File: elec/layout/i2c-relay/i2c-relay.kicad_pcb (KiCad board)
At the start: 2 copper layers, 7 parts, among them U2 10kΩ ±1% 62.5mW, U3 1kΩ ±1% 62.5mW, U5 1kΩ ±1% 62.5mW

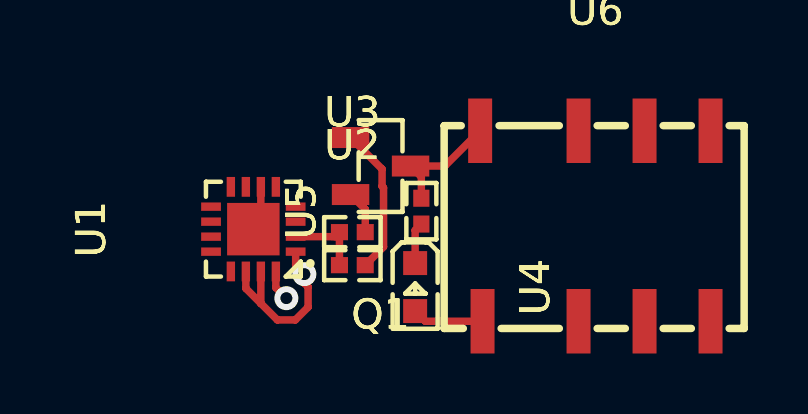
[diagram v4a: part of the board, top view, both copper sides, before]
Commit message: core layout, rebuild modules with compiler updates
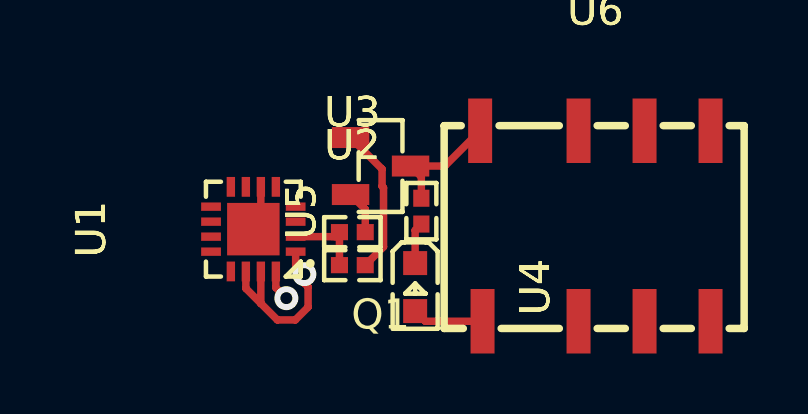
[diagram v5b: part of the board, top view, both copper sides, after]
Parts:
- Q1: footprint lib:SOT-23-3_L2.9-W1.3-P1.90-LS2.4-BR -> atopile:SOT-23-3_L2.9-W1.3-P1.90-LS2.4-BR-688f29
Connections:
- net gate renamed relay.fet.footprint.pins[0].net-net
- Q1 pad 2: gnd-1 -> gnd-3
- U1 pad 16: gnd-2 -> gnd-1
- U1 pad 17: gnd-2 -> gnd-1
- U1 pad 3: gpio_expander-net-3 -> gpio_expander-net-5
- U1 pad 4: gpio_expander-net-2 -> gpio_expander-net-6
- U1 pad 5: gpio_expander-net -> gpio_expander-net-3
- U1 pad 6: gnd-2 -> gnd-1
- U1 pad 7: gpio_expander-net-1 -> gpio_expander-net
- U1 pad 8: gpio_expander-net-6 -> gpio_expander-net-1
- U1 pad 9: gpio_expander-net-5 -> gpio_expander-net-2
- U3 pad 2: gnd-1 -> gnd-3
- U6 pad 4: gnd-3 -> gnd-2
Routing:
- net gnd-2: track 2.55 -> 0.00 mm, vias 1 -> 0
- net gnd-3: track 0.00 -> 1.46 mm
- net gnd-1: track 1.46 -> 2.55 mm, vias 0 -> 1
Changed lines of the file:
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@@
             (outputdirectory "")))
     (net 0 "")
-    (net 1 "gpio_expander-net-2")
+    (net 1 "gpio_expander-net-6")
     (net 2 "line-1")
     (net 3 "gpio_expander-net-4")
     (net 4 "hv")
-    (net 5 "gpio_expander-net-1")
-    (net 6 "gpio_expander-net-5")
+    (net 5 "gpio_expander-net")
+    (net 6 "gpio_expander-net-2")
     (net 7 "anode")
     (net 8 "input")
     (net 9 "gnd")
     (net 10 "INT")
-    (net 11 "gpio_expander-net-6")
+    (net 11 "gpio_expander-net-1")
     (net 12 "VCCI")
     (net 13 "hv-1")
     (net 14 "line")
-    (net 15 "gpio_expander-net")
-    (net 16 "gnd-3")
-    (net 17 "gnd-1")
+    (net 15 "gpio_expander-net-3")
+    (net 16 "gnd-2")
+    (net 17 "gnd-3")
     (net 18 "cathode")
     (net 19 "relay-gnd")
-    (net 20 "gate")
-    (net 21 "gpio_expander-net-3")
-    (net 22 "gnd-2")
+    (net 20 "relay.fet.footprint.pins[0].net-net")
+    (net 21 "gpio_expander-net-5")
+    (net 22 "gnd-1")
     (footprint "atopile:R0402-56259e"
         (layer "F.Cu")
@@
             (layers "F.Cu" "F.Paste" "F.Mask")
             (remove_unused_layers no)
-            (net 17 "gnd-1")))
+            (net 17 "gnd-3")))
     (footprint "lib:LED0603-RD"
         (layer "F.Cu")
@@
             (layers "F.Cu" "F.Paste" "F.Mask")
             (remove_unused_layers no)
-            (net 16 "gnd-3"))
+            (net 16 "gnd-2"))
         (pad "5" smd rect
             (at 3.84 -3.18 0)
@@
             (rotate
                 (xyz 0 0 0))))
-    (footprint "lib:SOT-23-3_L2.9-W1.3-P1.90-LS2.4-BR"
+    (footprint "atopile:SOT-23-3_L2.9-W1.3-P1.90-LS2.4-BR-688f29"
         (layer "F.Cu")
         (at 126.940774 90.496502 180)
@@
                 (font
                     (size 1 1)
-                    (thickness 0.15))))
+                    (thickness 0.15))
+                (hide no)))
         (property "Value" ""
-            (at 0 4.95 180)
+            (at 0 4.95 0)
             (layer "F.Fab")
             (hide no)
@@
                 (font
                     (size 1 1)
-                    (thickness 0.15))))
-        (property "Footprint" "lib:SOT-23-3_L2.9-W1.3-P1.90-LS2.4-BR"
+                    (thickness 0.15))
+                (hide no)))
+        (property "Footprint" "atopile:SOT-23-3_L2.9-W1.3-P1.90-LS2.4-BR-688f29"
             (at 0 0 180)
             (layer "User.9")
@@
                     (size 1.27 1.27)
                     (thickness 0.15))))
-        (property "__atopile_lib_fp_hash__" "031e619a-ffcb-a184-252f-a1621c6dde28"
-            (at 0 0 180)
+        (property "__atopile_lib_fp_hash__" "402f7197-01b9-8c53-5b79-21ffe1930bc8"
+            (at 0 0 0)
             (layer "User.9")
             (hide yes)
@@
         (attr smd)
         (fp_line
+            (start 0.73 -1.53)
+            (end -0.73 -1.53)
+            (stroke
+                (width 0.15)
+                (type solid))
+            (layer "F.SilkS")
+)
+        (fp_line
+            (start -0.73 -1.53)
+            (end -0.73 -0.49)
+            (stroke
+                (width 0.15)
+                (type solid))
+            (layer "F.SilkS")
+)
+        (fp_line
             (start 0.73 1.53)
             (end -0.73 1.53)
@@
 )
         (fp_line
+            (start -0.73 1.53)
+            (end -0.73 0.49)
+            (stroke
+                (width 0.15)
+                (type solid))
+            (layer "F.SilkS")
+)
+        (fp_line
             (start 0.73 -0.46)
             (end 0.73 0.46)
@@
             (layer "F.SilkS")
 )
-        (fp_line
-            (start 0.73 -1.53)
-            (end -0.73 -1.53)
-            (stroke
-                (width 0.15)
-                (type solid))
-            (layer "F.SilkS")
-)
-        (fp_line
-            (start -0.73 1.53)
-            (end -0.73 0.49)
-            (stroke
-                (width 0.15)
-                (type solid))
-            (layer "F.SilkS")
-)
-        (fp_line
-            (start -0.73 -1.53)
-            (end -0.73 -0.49)
-            (stroke
-                (width 0.15)
-                (type solid))
-            (layer "F.SilkS")
+        (fp_circle
+            (center 1.2 1.45)
+            (end 1.23 1.45)
+            (stroke
+                (width 0.06)
+                (type solid))
+            (fill none)
+            (layer "F.Fab")
 )
         (fp_circle
@@
             (layer "Cmts.User")
 )
-        (fp_circle
-            (center 1.2 1.45)
-            (end 1.23 1.45)
-            (stroke
-                (width 0.06)
-                (type solid))
-            (fill none)
-            (layer "F.Fab")
-)
-        (fp_text user "${REFERENCE}"
-            (at 0 -4.95 180)
-            (layer "F.SilkS")
+        (fp_text user "%R"
+            (at 0 0 0)
+            (layer "F.Fab")
             (effects
                 (font
@@
             (unlocked no))
         (fp_text user "${REFERENCE}"
-            (at 0 0 180)
-            (layer "F.Fab")
+            (at 0 -4.95 0)
+            (layer "F.SilkS")
             (effects
                 (font
@@
             (layers "F.Cu" "F.Paste" "F.Mask")
             (remove_unused_layers no)
-            (net 20 "gate"))
+            (net 20 "relay.fet.footprint.pins[0].net-net"))
         (pad "2" smd rect
             (at 1 -0.95 180)
@@
             (layers "F.Cu" "F.Paste" "F.Mask")
             (remove_unused_layers no)
-            (net 17 "gnd-1"))
+            (net 17 "gnd-3"))
         (pad "3" smd rect
             (at -1 0 180)
@@
             (layers "F.Cu" "F.Paste" "F.Mask")
             (remove_unused_layers no)
-            (net 19 "relay-gnd"))
-        (model "/Users/narayanpowderly/projects/hil-blocks/build/footprints/footprints.3dshapes/SOT-23-3P_L2.9-W1.3-H1.0-LS2.4-P0.95.step"
-            (offset
-                (xyz -861.57 843.28 0))
-            (scale
-                (xyz 1 1 1))
-            (rotate
-                (xyz 0 0 180))))
+            (net 19 "relay-gnd")))
     (footprint "lib:QFN-16_L3.0-W3.0-P0.50-BL-EP1.7"
         (layer "F.Cu")
@@
             (layers "F.Cu" "F.Paste" "F.Mask")
             (remove_unused_layers no)
-            (net 21 "gpio_expander-net-3"))
+            (net 21 "gpio_expander-net-5"))
         (pad "4" smd rect
             (at 0.75 1.41 90)
@@
             (layers "F.Cu" "F.Paste" "F.Mask")
             (remove_unused_layers no)
-            (net 1 "gpio_expander-net-2"))
+            (net 1 "gpio_expander-net-6"))
         (pad "5" smd rect
             (at 1.41 0.75 90)
@@
             (layers "F.Cu" "F.Paste" "F.Mask")
             (remove_unused_layers no)
-            (net 15 "gpio_expander-net"))
+            (net 15 "gpio_expander-net-3"))
         (pad "6" smd rect
             (at 1.41 0.25 90)
@@
             (layers "F.Cu" "F.Paste" "F.Mask")
             (remove_unused_layers no)
-            (net 22 "gnd-2"))
+            (net 22 "gnd-1"))
         (pad "7" smd rect
             (at 1.41 -0.25 90)
@@
             (layers "F.Cu" "F.Paste" "F.Mask")
             (remove_unused_layers no)
-            (net 5 "gpio_expander-net-1"))
+            (net 5 "gpio_expander-net"))
         (pad "8" smd rect
             (at 1.41 -0.75 90)
@@
             (layers "F.Cu" "F.Paste" "F.Mask")
             (remove_unused_layers no)
-            (net 11 "gpio_expander-net-6"))
+            (net 11 "gpio_expander-net-1"))
         (pad "9" smd rect
             (at 0.75 -1.41 90)
@@
             (layers "F.Cu" "F.Paste" "F.Mask")
             (remove_unused_layers no)
-            (net 6 "gpio_expander-net-5"))
+            (net 6 "gpio_expander-net-2"))
         (pad "10" smd rect
             (at 0.25 -1.41 90)
@@
             (layers "F.Cu" "F.Paste" "F.Mask")
             (remove_unused_layers no)
-            (net 22 "gnd-2"))
+            (net 22 "gnd-1"))
         (pad "17" smd rect
             (at 0 0 90)
@@
             (layers "F.Cu" "F.Paste" "F.Mask")
             (remove_unused_layers no)
-            (net 22 "gnd-2"))
+            (net 22 "gnd-1"))
         (model "/Users/narayanpowderly/projects/hil-blocks/build/footprints/footprints.3dshapes/QFN-16_L3.0-W3.0-H0.9-P0.50.step"
             (offset
@@
             (layers "F.Cu" "F.Paste" "F.Mask")
             (remove_unused_layers no)
-            (net 20 "gate")))
+            (net 20 "relay.fet.footprint.pins[0].net-net")))
     (via
         (at 124.4 94.1)

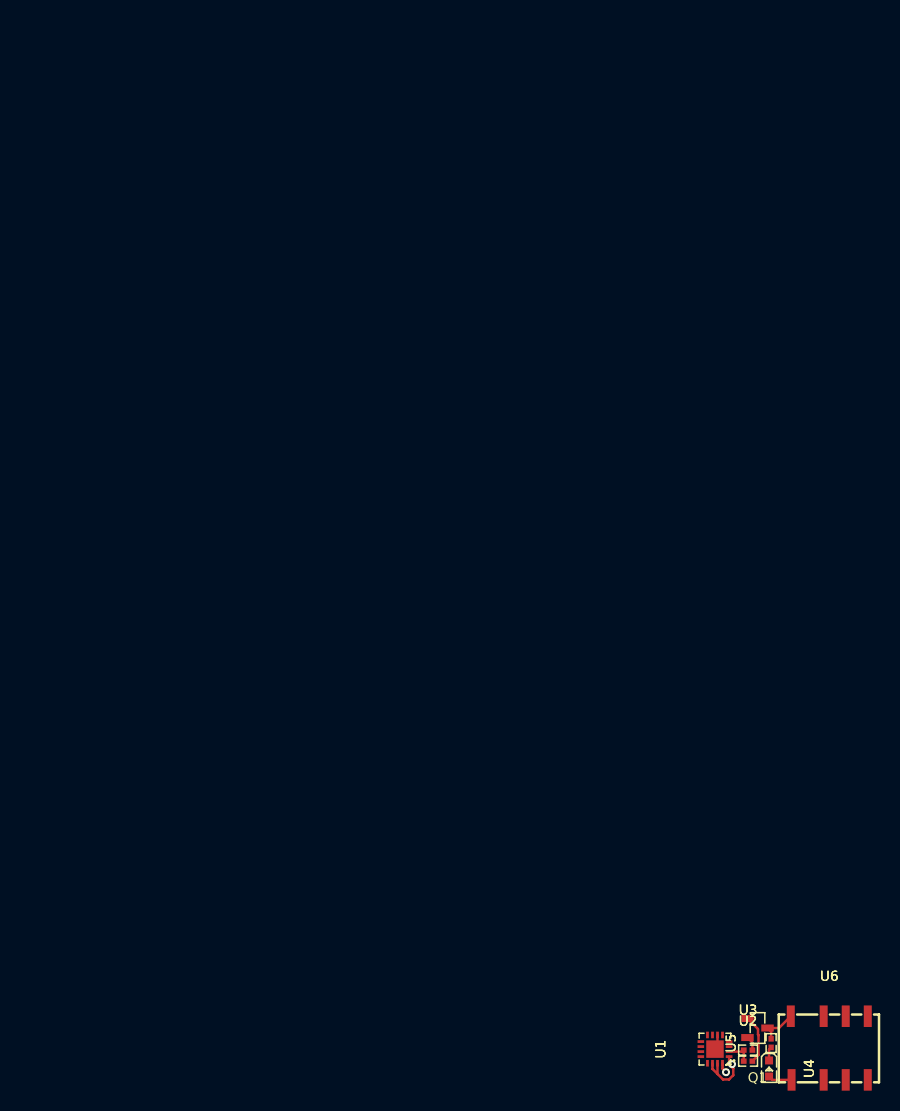
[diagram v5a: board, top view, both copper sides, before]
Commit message: analog out, relay, cleanup
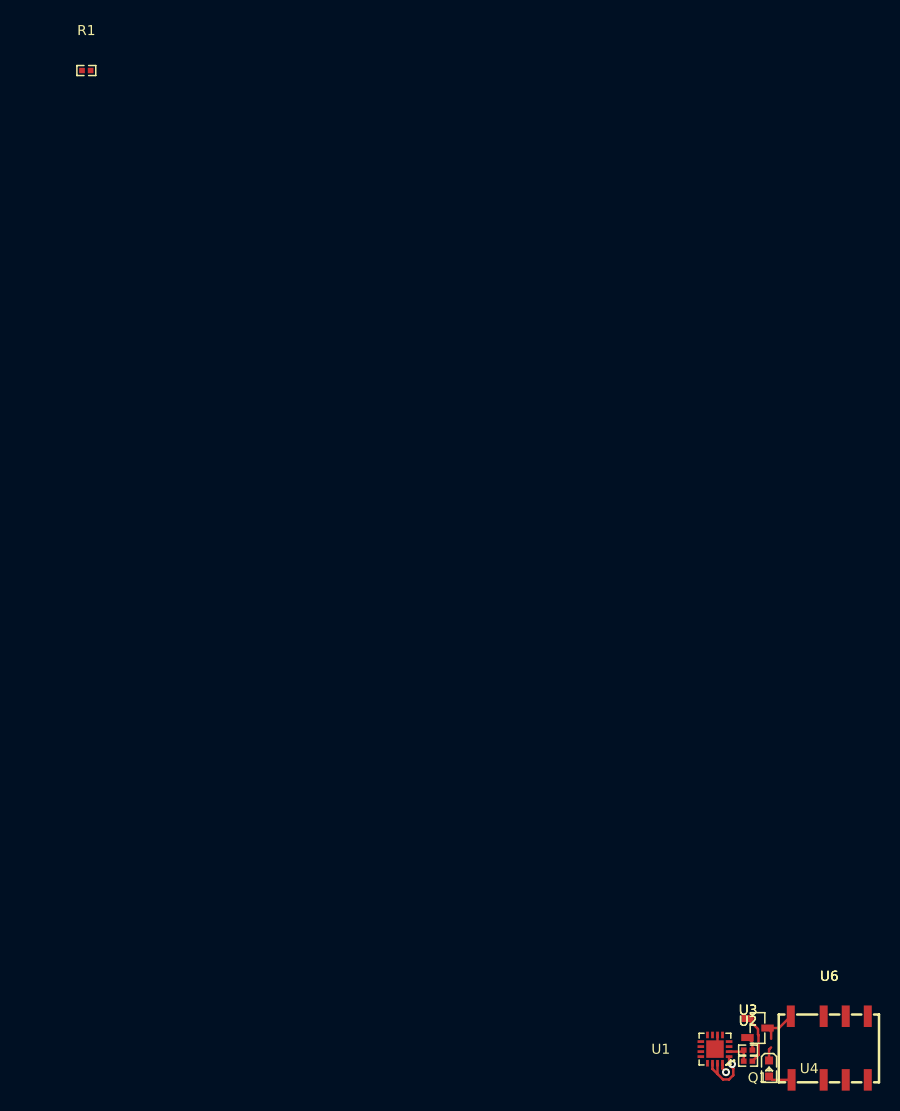
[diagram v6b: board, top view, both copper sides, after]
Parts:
- removed U5: 1kΩ ±1% 62.5mW, atopile:R0402-56259e
- added R1: 1kΩ ±1% 62.5mW, atopile:R0402-56259e, F.Cu at (60.0, -5.00)
- U1: footprint lib:QFN-16_L3.0-W3.0-P0.50-BL-EP1.7 -> atopile:QFN-16_L3.0-W3.0-P0.50-BL-EP1.7-3a4c56
- U4: footprint lib:LED0603-RD -> atopile:LED0603-RD-c81ffb
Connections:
- net VCCI renamed RESET
- net anode renamed hv-2
- net relay.fet.footprint.pins[0].net-net renamed gate
- U1 pad 10: gpio_expander-net-4 -> gpio_expander-net-2
- U1 pad 13: line -> line-2
- U1 pad 16: gnd-1 -> gnd-2
- U1 pad 17: gnd-1 -> gnd-2
- U1 pad 2: input -> line
- U1 pad 3: gpio_expander-net-5 -> gpio_expander-net-6
- U1 pad 4: gpio_expander-net-6 -> gpio_expander-net-4
- U1 pad 5: gpio_expander-net-3 -> gpio_expander-net-1
- U1 pad 6: gnd-1 -> gnd-2
- U1 pad 7: gpio_expander-net -> gpio_expander-net-3
- U1 pad 8: gpio_expander-net-1 -> gpio_expander-net-5
- U1 pad 9: gpio_expander-net-2 -> gpio_expander-net
- U2 pad 1: input -> line
- U3 pad 1: input -> line
- U6 pad 4: gnd-2 -> gnd-1
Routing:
- net (no net): track 0.00 -> 5.42 mm
- net relay-gnd: track 4.03 -> 0.00 mm
- net line: track 0.00 -> 2.62 mm
- net input: track 2.62 -> 0.00 mm
- net gnd-2: track 0.00 -> 2.55 mm, vias 0 -> 1
- net gnd-1: track 2.55 -> 0.00 mm, vias 1 -> 0
- net cathode: track 1.39 -> 0.00 mm

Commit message: Everything builds
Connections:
- net RESET renamed VCCP
- Q1 pad 2: gnd-3 -> gnd
- U1 pad 10: gpio_expander-net-2 -> gpio_expander-net-5
- U1 pad 16: gnd-2 -> gnd-1
- U1 pad 17: gnd-2 -> gnd-1
- U1 pad 3: gpio_expander-net-6 -> gpio_expander-net
- U1 pad 4: gpio_expander-net-4 -> gpio_expander-net-3
- U1 pad 5: gpio_expander-net-1 -> gpio_expander-net-6
- U1 pad 6: gnd-2 -> gnd-1
- U1 pad 7: gpio_expander-net-3 -> gpio_expander-net-2
- U1 pad 8: gpio_expander-net-5 -> gpio_expander-net-4
- U1 pad 9: gpio_expander-net -> gpio_expander-net-1
- U3 pad 2: gnd-3 -> gnd
- U4 pad 2: hv-2 -> hv
- U6 pad 1: hv-2 -> hv
- U6 pad 3: gnd -> gnd-2
- U6 pad 4: gnd-1 -> gnd-3
- U6 pad 5: hv-1 -> hv-2
- U6 pad 6: hv -> hv-1
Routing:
- net gnd-2: track 2.55 -> 0.00 mm, vias 1 -> 0
- net gnd-1: track 0.00 -> 2.55 mm, vias 0 -> 1
- net hv-2: track 2.39 -> 0.00 mm
- net hv: track 0.00 -> 2.39 mm
- net gnd-3: track 1.46 -> 0.00 mm
- net gnd: track 0.00 -> 1.46 mm
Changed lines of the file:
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@@
             (outputdirectory "")))
     (net 0 "")
-    (net 1 "gpio_expander-net-4")
+    (net 1 "gpio_expander-net-3")
     (net 2 "line-1")
-    (net 3 "gpio_expander-net-2")
-    (net 4 "hv")
-    (net 5 "gpio_expander-net-3")
-    (net 6 "gpio_expander-net")
-    (net 7 "hv-2")
+    (net 3 "gpio_expander-net-5")
+    (net 4 "hv-1")
+    (net 5 "gpio_expander-net-2")
+    (net 6 "gpio_expander-net-1")
+    (net 7 "hv")
     (net 8 "line")
-    (net 9 "gnd")
+    (net 9 "gnd-2")
     (net 10 "INT")
-    (net 11 "gpio_expander-net-5")
-    (net 12 "RESET")
-    (net 13 "hv-1")
+    (net 11 "gpio_expander-net-4")
+    (net 12 "VCCP")
+    (net 13 "hv-2")
     (net 14 "line-2")
-    (net 15 "gpio_expander-net-1")
-    (net 16 "gnd-1")
-    (net 17 "gnd-3")
+    (net 15 "gpio_expander-net-6")
+    (net 16 "gnd-3")
+    (net 17 "gnd")
     (net 20 "gate")
-    (net 21 "gpio_expander-net-6")
-    (net 22 "gnd-2")
+    (net 21 "gpio_expander-net")
+    (net 22 "gnd-1")
     (net 23 "relay-gnd")
     (net 24 "cathode")
@@
             (layers "F.Cu" "F.Paste" "F.Mask")
             (remove_unused_layers no)
-            (net 17 "gnd-3")))
+            (net 17 "gnd")))
     (footprint "atopile:LED0603-RD-c81ffb"
         (layer "F.Cu")
@@
             (layers "F.Cu" "F.Paste" "F.Mask")
             (remove_unused_layers no)
-            (net 7 "hv-2"))
+            (net 7 "hv"))
         (pad "1" smd rect
             (at -0.8 0 0)
@@
             (layers "F.Cu" "F.Paste" "F.Mask")
             (remove_unused_layers no)
-            (net 7 "hv-2"))
+            (net 7 "hv"))
         (pad "2" smd rect
             (at -0.56 3.17 0)
@@
             (layers "F.Cu" "F.Paste" "F.Mask")
             (remove_unused_layers no)
-            (net 9 "gnd"))
+            (net 9 "gnd-2"))
         (pad "4" smd rect
             (at 3.84 3.17 0)
@@
             (layers "F.Cu" "F.Paste" "F.Mask")
             (remove_unused_layers no)
-            (net 16 "gnd-1"))
+            (net 16 "gnd-3"))
         (pad "5" smd rect
             (at 3.84 -3.18 0)
@@
             (layers "F.Cu" "F.Paste" "F.Mask")
             (remove_unused_layers no)
-            (net 13 "hv-1"))
+            (net 13 "hv-2"))
         (pad "6" smd rect
             (at 1.64 -3.18 0)
@@
             (layers "F.Cu" "F.Paste" "F.Mask")
             (remove_unused_layers no)
-            (net 4 "hv"))
+            (net 4 "hv-1"))
         (pad "7" smd rect
             (at -0.56 -3.18 0)
@@
             (layers "F.Cu" "F.Paste" "F.Mask")
             (remove_unused_layers no)
-            (net 17 "gnd-3"))
+            (net 17 "gnd"))
         (pad "3" smd rect
             (at -1 0 180)
@@
             (layers "F.Cu" "F.Paste" "F.Mask")
             (remove_unused_layers no)
-            (net 12 "RESET"))
+            (net 12 "VCCP"))
         (pad "2" smd rect
             (at -0.25 1.41 90)
@@
             (layers "F.Cu" "F.Paste" "F.Mask")
             (remove_unused_layers no)
-            (net 21 "gpio_expander-net-6"))
+            (net 21 "gpio_expander-net"))
         (pad "4" smd rect
             (at 0.75 1.41 90)
@@
             (layers "F.Cu" "F.Paste" "F.Mask")
             (remove_unused_layers no)
-            (net 1 "gpio_expander-net-4"))
+            (net 1 "gpio_expander-net-3"))
         (pad "5" smd rect
             (at 1.41 0.75 90)
@@
             (layers "F.Cu" "F.Paste" "F.Mask")
             (remove_unused_layers no)
-            (net 15 "gpio_expander-net-1"))
+            (net 15 "gpio_expander-net-6"))
         (pad "6" smd rect
             (at 1.41 0.25 90)
@@
             (layers "F.Cu" "F.Paste" "F.Mask")
             (remove_unused_layers no)
-            (net 22 "gnd-2"))
+            (net 22 "gnd-1"))
         (pad "7" smd rect
             (at 1.41 -0.25 90)
@@
             (layers "F.Cu" "F.Paste" "F.Mask")
             (remove_unused_layers no)
-            (net 5 "gpio_expander-net-3"))
+            (net 5 "gpio_expander-net-2"))
         (pad "8" smd rect
             (at 1.41 -0.75 90)
@@
             (layers "F.Cu" "F.Paste" "F.Mask")
             (remove_unused_layers no)
-            (net 11 "gpio_expander-net-5"))
+            (net 11 "gpio_expander-net-4"))
         (pad "9" smd rect
             (at 0.75 -1.41 90)
@@
             (layers "F.Cu" "F.Paste" "F.Mask")
             (remove_unused_layers no)
-            (net 6 "gpio_expander-net"))
+            (net 6 "gpio_expander-net-1"))
         (pad "10" smd rect
             (at 0.25 -1.41 90)
@@
             (layers "F.Cu" "F.Paste" "F.Mask")
             (remove_unused_layers no)
-            (net 3 "gpio_expander-net-2"))
+            (net 3 "gpio_expander-net-5"))
         (pad "11" smd rect
             (at -0.25 -1.41 90)
@@
             (layers "F.Cu" "F.Paste" "F.Mask")
             (remove_unused_layers no)
-            (net 12 "RESET"))
+            (net 12 "VCCP"))
         (pad "15" smd rect
             (at -1.41 0.25 90)
@@
             (layers "F.Cu" "F.Paste" "F.Mask")
             (remove_unused_layers no)
-            (net 12 "RESET"))
+            (net 12 "VCCP"))
         (pad "16" smd rect
             (at -1.41 0.75 90)
@@
             (layers "F.Cu" "F.Paste" "F.Mask")
             (remove_unused_layers no)
-            (net 22 "gnd-2"))
+            (net 22 "gnd-1"))
         (pad "17" smd rect
             (at 0 0 90)
@@
             (layers "F.Cu" "F.Paste" "F.Mask")
             (remove_unused_layers no)
-            (net 22 "gnd-2")))
+            (net 22 "gnd-1")))
     (footprint "atopile:R0402-56259e"
         (layer "F.Cu")
